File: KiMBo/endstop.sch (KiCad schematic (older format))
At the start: 19 parts

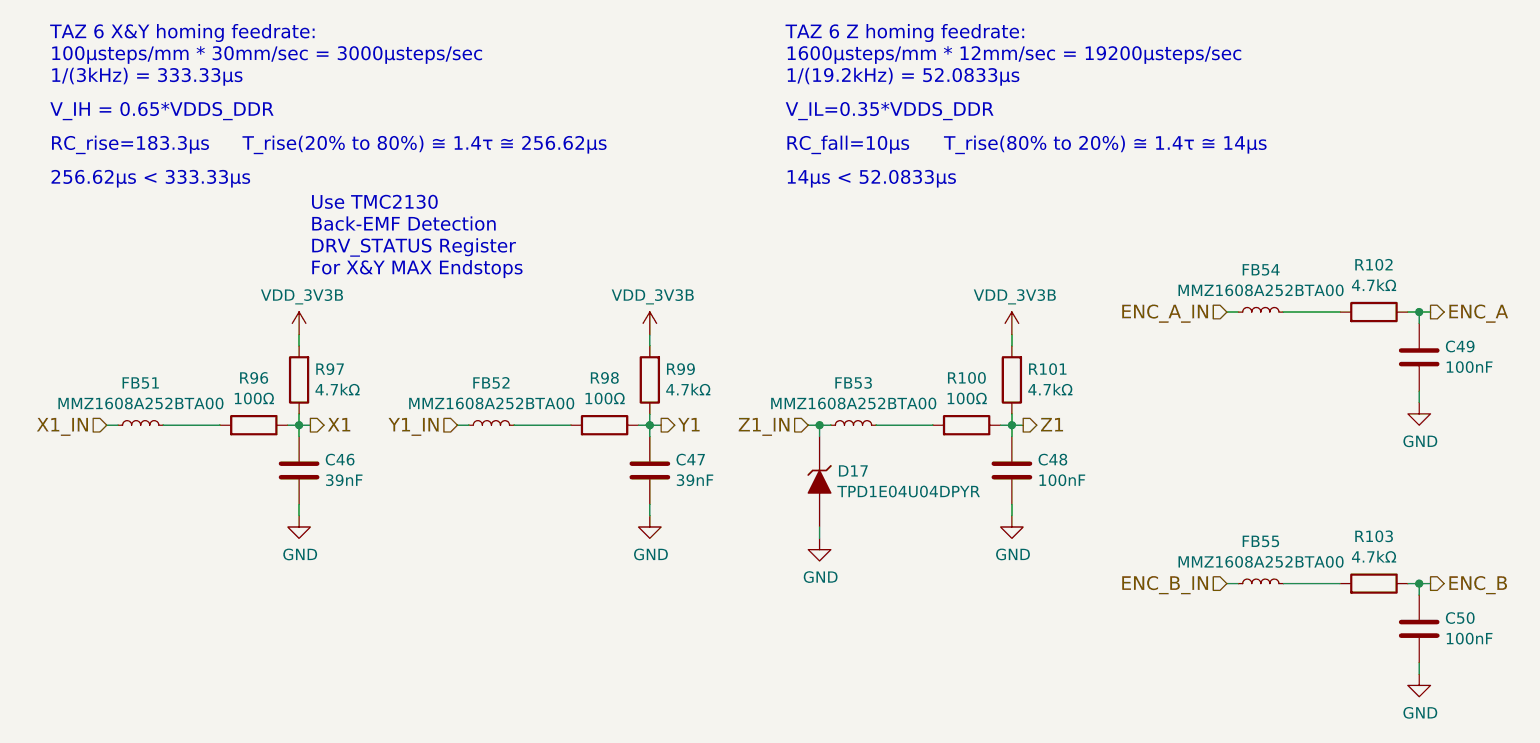
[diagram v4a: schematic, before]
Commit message: Remove the unneeded oscillator, track down which components are underneath the OSD3358 and put them on the top
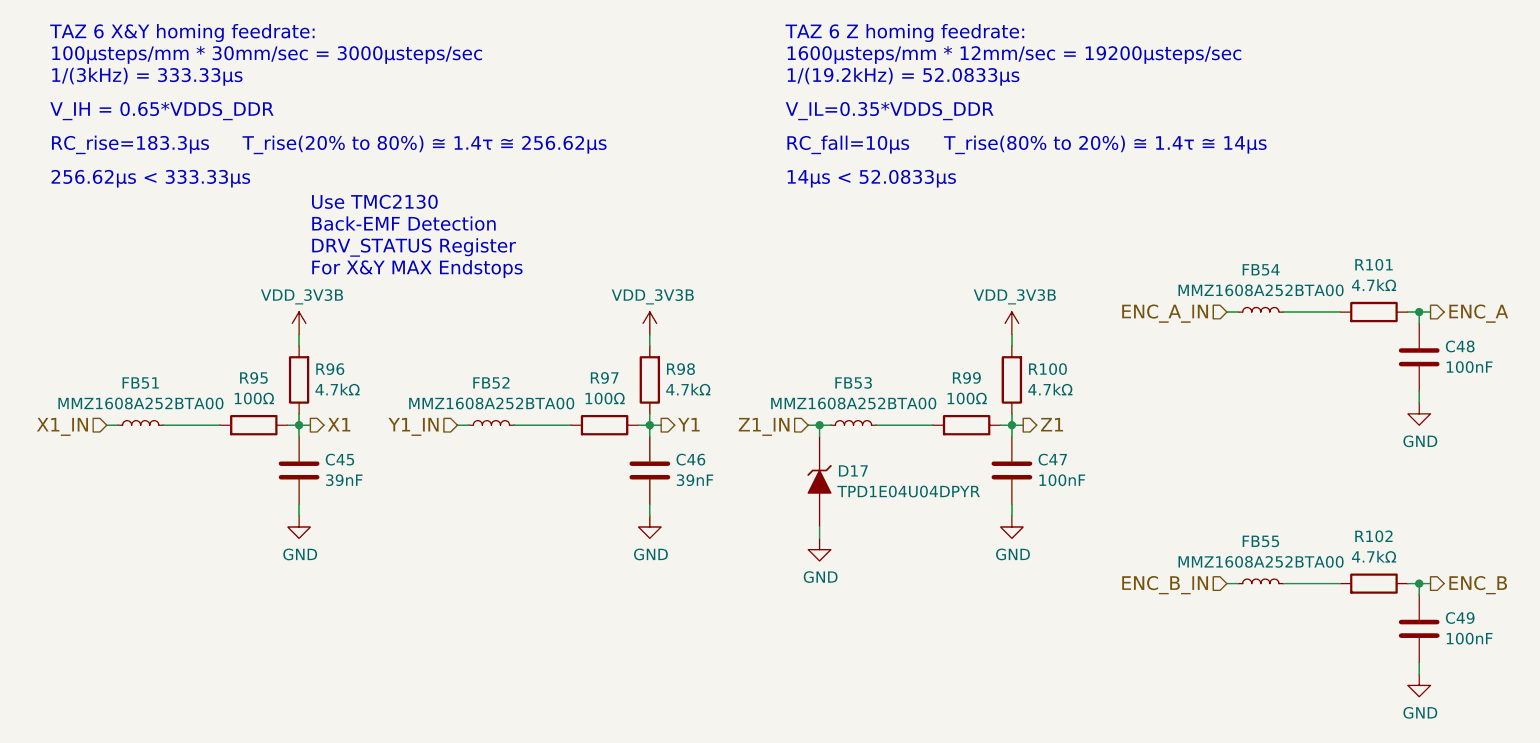
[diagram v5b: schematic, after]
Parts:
- renumbered C46 to C45, C47 to C46, C48 to C47, C49 to C48, C50 to C49, R101 to R100, R102 to R101, R103 to R102, R96 to R95, R97 to R96, R98 to R97, R99 to R98, R100 to R99
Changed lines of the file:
@@
 X1
 $Comp
-L C C46
+L C C45
 U 1 1 58129032
 P 6150 5500
-F 0 "C46" H 6264 5546 50  0000 L CNN
+F 0 "C45" H 6264 5546 50  0000 L CNN
 F 1 "39nF" H 6264 5455 50  0000 L CNN
 F 2 "Capacitors_SMD:C_0603" H 6188 5350 50  0001 C CNN
@@
 $EndComp
 $Comp
-L R R97
+L R R96
 U 1 1 58129040
 P 6150 5100
-F 0 "R97" H 6081 5054 50  0000 R CNN
+F 0 "R96" H 6081 5054 50  0000 R CNN
 F 1 "4.7kΩ" H 6081 5145 50  0000 R CNN
 F 2 "Resistors_SMD:R_0603" V 6080 5100 50  0001 C CNN
@@
 	6150 4950 6150 4900
 $Comp
-L R R96
+L R R95
 U 1 1 5812D30B
 P 5950 5300
-F 0 "R96" V 6157 5300 50  0000 C CNN
+F 0 "R95" V 6157 5300 50  0000 C CNN
 F 1 "100Ω" V 6066 5300 50  0000 C CNN
 F 2 "Resistors_SMD:R_0603" V 5880 5300 50  0001 C CNN
@@
 Y1
 $Comp
-L C C47
+L C C46
 U 1 1 589415E7
 P 7700 5500
-F 0 "C47" H 7814 5546 50  0000 L CNN
+F 0 "C46" H 7814 5546 50  0000 L CNN
 F 1 "39nF" H 7814 5455 50  0000 L CNN
 F 2 "Capacitors_SMD:C_0603" H 7738 5350 50  0001 C CNN
@@
 $EndComp
 $Comp
-L R R99
+L R R98
 U 1 1 589415EE
 P 7700 5100
-F 0 "R99" H 7631 5054 50  0000 R CNN
+F 0 "R98" H 7631 5054 50  0000 R CNN
 F 1 "4.7kΩ" H 7631 5145 50  0000 R CNN
 F 2 "Resistors_SMD:R_0603" V 7630 5100 50  0001 C CNN
@@
 	7700 4950 7700 4900
 $Comp
-L R R98
+L R R97
 U 1 1 58941610
 P 7500 5300
-F 0 "R98" V 7707 5300 50  0000 C CNN
+F 0 "R97" V 7707 5300 50  0000 C CNN
 F 1 "100Ω" V 7616 5300 50  0000 C CNN
 F 2 "Resistors_SMD:R_0603" V 7430 5300 50  0001 C CNN
@@
 Z1
 $Comp
-L C C48
+L C C47
 U 1 1 58941879
 P 9300 5500
-F 0 "C48" H 9414 5546 50  0000 L CNN
+F 0 "C47" H 9414 5546 50  0000 L CNN
 F 1 "100nF" H 9414 5455 50  0000 L CNN
 F 2 "Capacitors_SMD:C_0603" H 9338 5350 50  0001 C CNN
@@
 $EndComp
 $Comp
-L R R101
+L R R100
 U 1 1 58941880
 P 9300 5100
-F 0 "R101" H 9231 5054 50  0000 R CNN
+F 0 "R100" H 9231 5054 50  0000 R CNN
 F 1 "4.7kΩ" H 9231 5145 50  0000 R CNN
 F 2 "Resistors_SMD:R_0603" V 9230 5100 50  0001 C CNN
@@
 	9300 4950 9300 4900
 $Comp
-L R R100
+L R R99
 U 1 1 589418A2
 P 9100 5300
-F 0 "R100" V 9307 5300 50  0000 C CNN
+F 0 "R99" V 9307 5300 50  0000 C CNN
 F 1 "100Ω" V 9216 5300 50  0000 C CNN
 F 2 "Resistors_SMD:R_0603" V 9030 5300 50  0001 C CNN
@@
 ENC_A
 $Comp
-L C C49
+L C C48
 U 1 1 5894C248
 P 11100 5000
-F 0 "C49" H 11214 5046 50  0000 L CNN
+F 0 "C48" H 11214 5046 50  0000 L CNN
 F 1 "100nF" H 11214 4955 50  0000 L CNN
 F 2 "Capacitors_SMD:C_0603" H 11138 4850 50  0001 C CNN
@@
 	11100 6000 11100 6050
 $Comp
-L C C50
+L C C49
 U 1 1 5894C2A4
 P 11100 6200
-F 0 "C50" H 11214 6246 50  0000 L CNN
+F 0 "C49" H 11214 6246 50  0000 L CNN
 F 1 "100nF" H 11214 6155 50  0000 L CNN
 F 2 "Capacitors_SMD:C_0603" H 11138 6050 50  0001 C CNN
@@
 ENC_B_IN
 $Comp
-L VDD_3V3B #PWR0145
+L VDD_3V3B #PWR0143
 U 1 1 59E67523
 P 6150 4900
-F 0 "#PWR0145" H 6150 4750 50  0001 C CNN
+F 0 "#PWR0143" H 6150 4750 50  0001 C CNN
 F 1 "VDD_3V3B" H 6165 5073 50  0000 C CNN
 F 2 "" H 6150 4900 50  0000 C CNN
@@
 $EndComp
 $Comp
-L VDD_3V3B #PWR0146
+L VDD_3V3B #PWR0144
 U 1 1 59E6755C
 P 7700 4900
-F 0 "#PWR0146" H 7700 4750 50  0001 C CNN
+F 0 "#PWR0144" H 7700 4750 50  0001 C CNN
 F 1 "VDD_3V3B" H 7715 5073 50  0000 C CNN
 F 2 "" H 7700 4900 50  0000 C CNN
@@
 $EndComp
 $Comp
-L VDD_3V3B #PWR0147
+L VDD_3V3B #PWR0145
 U 1 1 59E6758E
 P 9300 4900
-F 0 "#PWR0147" H 9300 4750 50  0001 C CNN
+F 0 "#PWR0145" H 9300 4750 50  0001 C CNN
 F 1 "VDD_3V3B" H 9315 5073 50  0000 C CNN
 F 2 "" H 9300 4900 50  0000 C CNN
@@
 	11050 6000 11150 6000
 $Comp
-L GND #PWR0148
+L GND #PWR0146
 U 1 1 59E68F88
 P 11100 5200
-F 0 "#PWR0148" H 11100 4950 50  0001 C CNN
+F 0 "#PWR0146" H 11100 4950 50  0001 C CNN
 F 1 "GND" H 11105 5027 50  0000 C CNN
 F 2 "" H 11100 5200 50  0000 C CNN
@@
 $EndComp
 $Comp
-L GND #PWR0149
+L GND #PWR0147
 U 1 1 59E68FBB
 P 11100 6400
-F 0 "#PWR0149" H 11100 6150 50  0001 C CNN
+F 0 "#PWR0147" H 11100 6150 50  0001 C CNN
 F 1 "GND" H 11105 6227 50  0000 C CNN
 F 2 "" H 11100 6400 50  0000 C CNN
@@
 $EndComp
 $Comp
-L GND #PWR0150
+L GND #PWR0148
 U 1 1 59E68FE7
 P 9300 5700
-F 0 "#PWR0150" H 9300 5450 50  0001 C CNN
+F 0 "#PWR0148" H 9300 5450 50  0001 C CNN
 F 1 "GND" H 9305 5527 50  0000 C CNN
 F 2 "" H 9300 5700 50  0000 C CNN
@@
 $EndComp
 $Comp
-L GND #PWR0151
+L GND #PWR0149
 U 1 1 59E69013
 P 7700 5700
-F 0 "#PWR0151" H 7700 5450 50  0001 C CNN
+F 0 "#PWR0149" H 7700 5450 50  0001 C CNN
 F 1 "GND" H 7705 5527 50  0000 C CNN
 F 2 "" H 7700 5700 50  0000 C CNN
@@
 $EndComp
 $Comp
-L GND #PWR0152
+L GND #PWR0150
 U 1 1 59E6903F
 P 6150 5700
-F 0 "#PWR0152" H 6150 5450 50  0001 C CNN
+F 0 "#PWR0150" H 6150 5450 50  0001 C CNN
 F 1 "GND" H 6155 5527 50  0000 C CNN
 F 2 "" H 6150 5700 50  0000 C CNN
@@
 	10300 6000 10250 6000
 $Comp
-L R R102
+L R R101
 U 1 1 5B2944CE
 P 10900 4800
-F 0 "R102" V 11107 4800 50  0000 C CNN
+F 0 "R101" V 11107 4800 50  0000 C CNN
 F 1 "4.7kΩ" V 11016 4800 50  0000 C CNN
 F 2 "Resistors_SMD:R_0603" V 10830 4800 50  0001 C CNN
@@
 $EndComp
 $Comp
-L R R103
+L R R102
 U 1 1 5B294BC6
 P 10900 6000
-F 0 "R103" V 11107 6000 50  0000 C CNN
+F 0 "R102" V 11107 6000 50  0000 C CNN
 F 1 "4.7kΩ" V 11016 6000 50  0000 C CNN
 F 2 "Resistors_SMD:R_0603" V 10830 6000 50  0001 C CNN
@@
 Connection ~ 8450 5300
 $Comp
-L GND #PWR0153
+L GND #PWR0151
 U 1 1 5B4EDFC5
 P 8450 5800
-F 0 "#PWR0153" H 8450 5550 50  0001 C CNN
+F 0 "#PWR0151" H 8450 5550 50  0001 C CNN
 F 1 "GND" H 8455 5627 50  0000 C CNN
 F 2 "" H 8450 5800 50  0000 C CNN

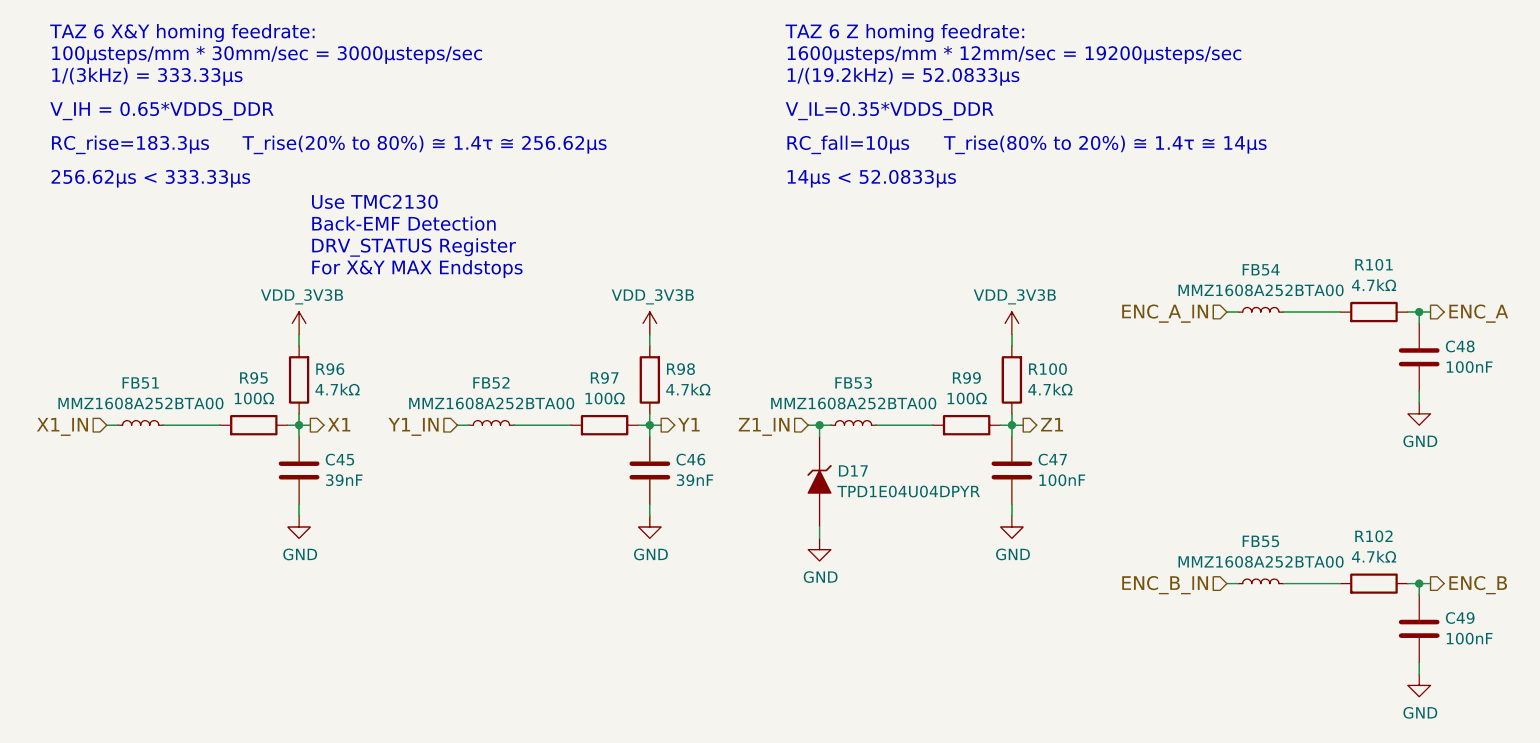
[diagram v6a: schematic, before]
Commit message: Complete parallel data bus routing from the eMMC to the CPU
Center the SiP on the PCB

Add LPFs at the I2Cs' SCL outputs
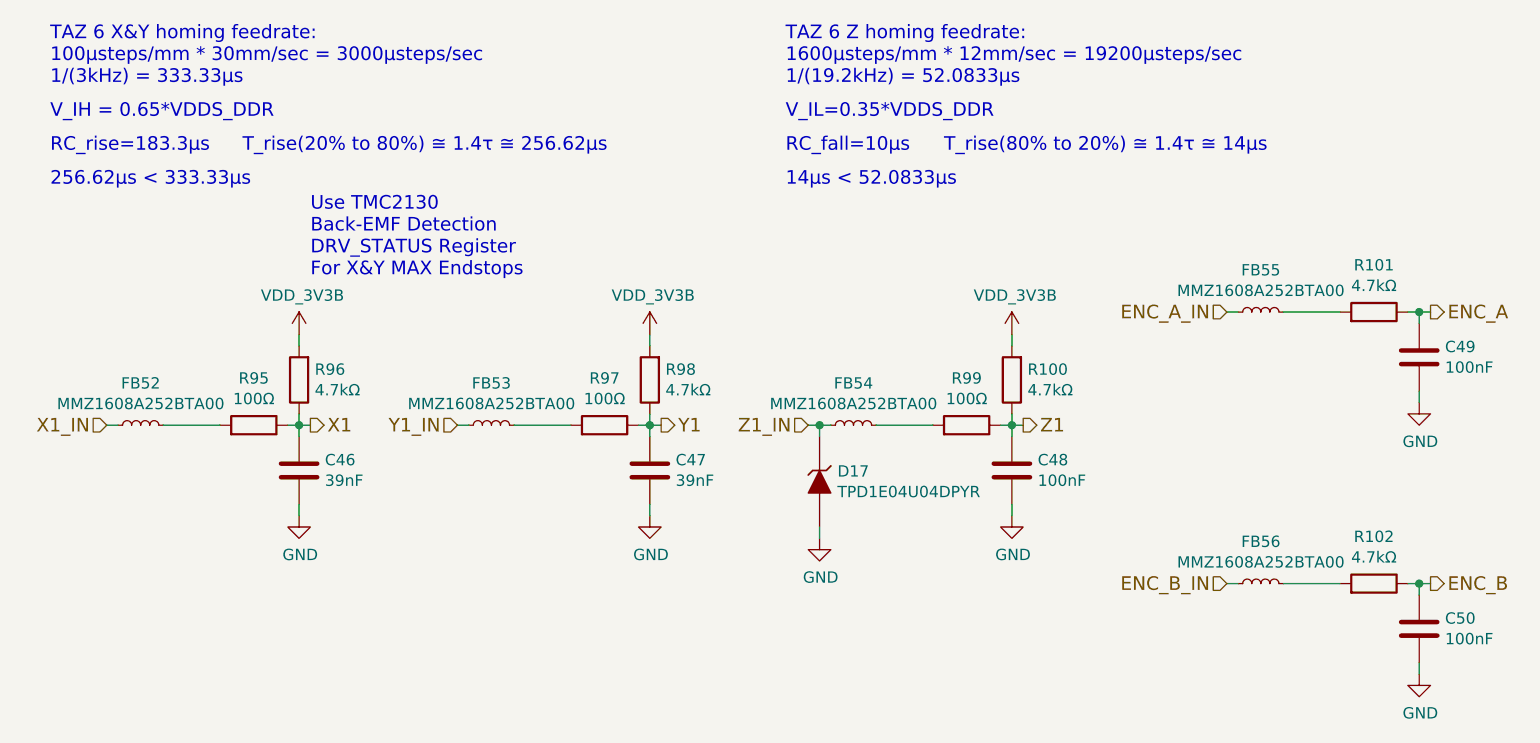
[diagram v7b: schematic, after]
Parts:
- renumbered C45 to C46, C46 to C47, C47 to C48, C48 to C49, C49 to C50, FB51 to FB52, FB52 to FB53, FB53 to FB54, FB54 to FB55, FB55 to FB56
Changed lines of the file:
@@
 X1
 $Comp
-L C C45
+L C C46
 U 1 1 58129032
 P 6150 5500
-F 0 "C45" H 6264 5546 50  0000 L CNN
+F 0 "C46" H 6264 5546 50  0000 L CNN
 F 1 "39nF" H 6264 5455 50  0000 L CNN
 F 2 "Capacitors_SMD:C_0603" H 6188 5350 50  0001 C CNN
@@
 Y1
 $Comp
-L C C46
+L C C47
 U 1 1 589415E7
 P 7700 5500
-F 0 "C46" H 7814 5546 50  0000 L CNN
+F 0 "C47" H 7814 5546 50  0000 L CNN
 F 1 "39nF" H 7814 5455 50  0000 L CNN
 F 2 "Capacitors_SMD:C_0603" H 7738 5350 50  0001 C CNN
@@
 Z1
 $Comp
-L C C47
+L C C48
 U 1 1 58941879
 P 9300 5500
-F 0 "C47" H 9414 5546 50  0000 L CNN
+F 0 "C48" H 9414 5546 50  0000 L CNN
 F 1 "100nF" H 9414 5455 50  0000 L CNN
 F 2 "Capacitors_SMD:C_0603" H 9338 5350 50  0001 C CNN
@@
 ENC_A
 $Comp
-L C C48
+L C C49
 U 1 1 5894C248
 P 11100 5000
-F 0 "C48" H 11214 5046 50  0000 L CNN
+F 0 "C49" H 11214 5046 50  0000 L CNN
 F 1 "100nF" H 11214 4955 50  0000 L CNN
 F 2 "Capacitors_SMD:C_0603" H 11138 4850 50  0001 C CNN
@@
 	11100 6000 11100 6050
 $Comp
-L C C49
+L C C50
 U 1 1 5894C2A4
 P 11100 6200
-F 0 "C49" H 11214 6246 50  0000 L CNN
+F 0 "C50" H 11214 6246 50  0000 L CNN
 F 1 "100nF" H 11214 6155 50  0000 L CNN
 F 2 "Capacitors_SMD:C_0603" H 11138 6050 50  0001 C CNN
@@
 ENC_B_IN
 $Comp
-L VDD_3V3B #PWR0143
+L VDD_3V3B #PWR0144
 U 1 1 59E67523
 P 6150 4900
-F 0 "#PWR0143" H 6150 4750 50  0001 C CNN
+F 0 "#PWR0144" H 6150 4750 50  0001 C CNN
 F 1 "VDD_3V3B" H 6165 5073 50  0000 C CNN
 F 2 "" H 6150 4900 50  0000 C CNN
@@
 $EndComp
 $Comp
-L VDD_3V3B #PWR0144
+L VDD_3V3B #PWR0145
 U 1 1 59E6755C
 P 7700 4900
-F 0 "#PWR0144" H 7700 4750 50  0001 C CNN
+F 0 "#PWR0145" H 7700 4750 50  0001 C CNN
 F 1 "VDD_3V3B" H 7715 5073 50  0000 C CNN
 F 2 "" H 7700 4900 50  0000 C CNN
@@
 $EndComp
 $Comp
-L VDD_3V3B #PWR0145
+L VDD_3V3B #PWR0146
 U 1 1 59E6758E
 P 9300 4900
-F 0 "#PWR0145" H 9300 4750 50  0001 C CNN
+F 0 "#PWR0146" H 9300 4750 50  0001 C CNN
 F 1 "VDD_3V3B" H 9315 5073 50  0000 C CNN
 F 2 "" H 9300 4900 50  0000 C CNN
@@
 	11050 6000 11150 6000
 $Comp
-L GND #PWR0146
+L GND #PWR0147
 U 1 1 59E68F88
 P 11100 5200
-F 0 "#PWR0146" H 11100 4950 50  0001 C CNN
+F 0 "#PWR0147" H 11100 4950 50  0001 C CNN
 F 1 "GND" H 11105 5027 50  0000 C CNN
 F 2 "" H 11100 5200 50  0000 C CNN
@@
 $EndComp
 $Comp
-L GND #PWR0147
+L GND #PWR0148
 U 1 1 59E68FBB
 P 11100 6400
-F 0 "#PWR0147" H 11100 6150 50  0001 C CNN
+F 0 "#PWR0148" H 11100 6150 50  0001 C CNN
 F 1 "GND" H 11105 6227 50  0000 C CNN
 F 2 "" H 11100 6400 50  0000 C CNN
@@
 $EndComp
 $Comp
-L GND #PWR0148
+L GND #PWR0149
 U 1 1 59E68FE7
 P 9300 5700
-F 0 "#PWR0148" H 9300 5450 50  0001 C CNN
+F 0 "#PWR0149" H 9300 5450 50  0001 C CNN
 F 1 "GND" H 9305 5527 50  0000 C CNN
 F 2 "" H 9300 5700 50  0000 C CNN
@@
 $EndComp
 $Comp
-L GND #PWR0149
+L GND #PWR0150
 U 1 1 59E69013
 P 7700 5700
-F 0 "#PWR0149" H 7700 5450 50  0001 C CNN
+F 0 "#PWR0150" H 7700 5450 50  0001 C CNN
 F 1 "GND" H 7705 5527 50  0000 C CNN
 F 2 "" H 7700 5700 50  0000 C CNN
@@
 $EndComp
 $Comp
-L GND #PWR0150
+L GND #PWR0151
 U 1 1 59E6903F
 P 6150 5700
-F 0 "#PWR0150" H 6150 5450 50  0001 C CNN
+F 0 "#PWR0151" H 6150 5450 50  0001 C CNN
 F 1 "GND" H 6155 5527 50  0000 C CNN
 F 2 "" H 6150 5700 50  0000 C CNN
@@
 	7100 5300 7350 5300
 $Comp
-L INDUCTOR_Small FB51
+L INDUCTOR_Small FB52
 U 1 1 5B28F416
 P 5450 5300
-F 0 "FB51" V 5635 5300 50  0000 C CNN
+F 0 "FB52" V 5635 5300 50  0000 C CNN
 F 1 "MMZ1608A252BTA00" V 5544 5300 50  0000 C CNN
 F 2 "KiMBo:Ferrite_Bead_0603" H 5450 5300 50  0001 C CNN
@@
 	5550 5300 5800 5300
 $Comp
-L INDUCTOR_Small FB54
+L INDUCTOR_Small FB55
 U 1 1 5B292FBD
 P 10400 4800
-F 0 "FB54" V 10585 4800 50  0000 C CNN
+F 0 "FB55" V 10585 4800 50  0000 C CNN
 F 1 "MMZ1608A252BTA00" V 10494 4800 50  0000 C CNN
 F 2 "KiMBo:Ferrite_Bead_0603" H 10400 4800 50  0001 C CNN
@@
 $EndComp
 $Comp
-L INDUCTOR_Small FB55
+L INDUCTOR_Small FB56
 U 1 1 5B293036
 P 10400 6000
-F 0 "FB55" V 10585 6000 50  0000 C CNN
+F 0 "FB56" V 10585 6000 50  0000 C CNN
 F 1 "MMZ1608A252BTA00" V 10494 6000 50  0000 C CNN
 F 2 "KiMBo:Ferrite_Bead_0603" H 10400 6000 50  0001 C CNN
@@
 Connection ~ 8450 5300
 $Comp
-L GND #PWR0151
+L GND #PWR0152
 U 1 1 5B4EDFC5
 P 8450 5800
-F 0 "#PWR0151" H 8450 5550 50  0001 C CNN
+F 0 "#PWR0152" H 8450 5550 50  0001 C CNN
 F 1 "GND" H 8455 5627 50  0000 C CNN
 F 2 "" H 8450 5800 50  0000 C CNN
@@
 	8450 5800 8450 5750
 $Comp
-L INDUCTOR_Small FB52
+L INDUCTOR_Small FB53
 U 1 1 5B9752EE
 P 7000 5300
-F 0 "FB52" V 7185 5300 50  0000 C CNN
+F 0 "FB53" V 7185 5300 50  0000 C CNN
 F 1 "MMZ1608A252BTA00" V 7094 5300 50  0000 C CNN
 F 2 "KiMBo:Ferrite_Bead_0603" H 7000 5300 50  0001 C CNN
@@
 $EndComp
 $Comp
-L INDUCTOR_Small FB53
+L INDUCTOR_Small FB54
 U 1 1 5B975719
 P 8600 5300
-F 0 "FB53" V 8785 5300 50  0000 C CNN
+F 0 "FB54" V 8785 5300 50  0000 C CNN
 F 1 "MMZ1608A252BTA00" V 8694 5300 50  0000 C CNN
 F 2 "KiMBo:Ferrite_Bead_0603" H 8600 5300 50  0001 C CNN
